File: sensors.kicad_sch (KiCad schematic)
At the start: 68 parts, among them J1 1-4, J2 5-8, Q1 2N3906, U1 ADG707, U2 OPA2340, U3 OPA2340

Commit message: changes for layout
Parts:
- removed Q1: 2N3906, Package_TO_SOT_THT:TO-92_Inline, symbol Transistor_BJT:2N3906
- added Q1: MMBT3906, Package_TO_SOT_SMD:SOT-23, symbol Transistor_BJT:MMBT3906
- R1, R10, R11, R12, R13, R14, R15, R16, R2, R3, R4, R5, R6, R7, R8, R9: footprint (none) -> Resistor_SMD:R_0603_1608Metric_Pad0.98x0.95mm_HandSolder
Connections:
- net +3V3: now also Q1.2 (E)
- net SENSOR_READY: now also Q1.3 (C)
- net at R18.2, U1.28 (DA): now also U2.3 (+); no longer U2.5 (+)
- net at R25.2: now also Q1.1 (B)
- net at R17.2, U1.2 (DB): now also U2.5 (+); no longer U2.3 (+)
- new net: R20.1, U2.1, U2.2 (-)
- new net: R19.1, U2.6 (-), U2.7
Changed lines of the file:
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@@
     (pin "2")
   )
-  (symbol (lib_id "Amplifier_Operational:OPA2340") (at 157.48 115.57 0) (unit 2)
+  (symbol (lib_id "Amplifier_Operational:OPA2340") (at 157.48 115.57 0) (unit 1)
     (in_bom yes) (on_board yes)
     (property "Reference" "U2" (id 0) (at 158.75 109.22 0))
@@
       (effects (font (size 1.27 1.27)) (justify left))
     )
-    (property "Footprint" "" (id 2) (at 78.232 184.15 90)
+    (property "Footprint" "Resistor_SMD:R_0603_1608Metric_Pad0.98x0.95mm_HandSolder" (id 2) (at 78.232 184.15 90)
       (effects (font (size 1.27 1.27)) hide)
     )
@@
     (pin "1")
     (pin "2")
+  )
+  (symbol (lib_id "Transistor_BJT:MMBT3906") (at 237.49 125.73 0) (mirror x) (unit 1)
+    (in_bom yes) (on_board yes)
+    (property "Reference" "Q1" (id 0) (at 228.6 128.27 0)
+      (effects (font (size 1.27 1.27)) (justify left))
+    )
+    (property "Value" "MMBT3906" (id 1) (at 228.6 130.81 0)
+      (effects (font (size 1.27 1.27)) (justify left))
+    )
+    (property "Footprint" "Package_TO_SOT_SMD:SOT-23" (id 2) (at 242.57 123.825 0)
+      (effects (font (size 1.27 1.27) italic) (justify left) hide)
+    )
+    (property "Datasheet" "https://www.onsemi.com/pub/Collateral/2N3906-D.PDF" (id 3) (at 237.49 125.73 0)
+      (effects (font (size 1.27 1.27)) (justify left) hide)
+    )
+    (pin "1")
+    (pin "2")
+    (pin "3")
   )
   (symbol (lib_id "power:+3V3") (at 128.27 82.55 0) (unit 1)
@@
       (effects (font (size 1.27 1.27)) (justify left))
     )
-    (property "Footprint" "" (id 2) (at 78.232 21.59 90)
+    (property "Footprint" "Resistor_SMD:R_0603_1608Metric_Pad0.98x0.95mm_HandSolder" (id 2) (at 78.232 21.59 90)
       (effects (font (size 1.27 1.27)) hide)
     )
@@
     (pin "2")
   )
-  (symbol (lib_id "Transistor_BJT:2N3906") (at 237.49 125.73 0) (mirror x) (unit 1)
-    (in_bom yes) (on_board yes)
-    (property "Reference" "Q1" (id 0) (at 229.87 129.54 0)
-      (effects (font (size 1.27 1.27)) (justify left))
-    )
-    (property "Value" "2N3906" (id 1) (at 229.87 132.08 0)
-      (effects (font (size 1.27 1.27)) (justify left))
-    )
-    (property "Footprint" "Package_TO_SOT_THT:TO-92_Inline" (id 2) (at 242.57 123.825 0)
-      (effects (font (size 1.27 1.27) italic) (justify left) hide)
-    )
-    (property "Datasheet" "https://www.onsemi.com/pub/Collateral/2N3906-D.PDF" (id 3) (at 237.49 125.73 0)
-      (effects (font (size 1.27 1.27)) (justify left) hide)
-    )
-    (pin "1")
-    (pin "2")
-    (pin "3")
-  )
   (symbol (lib_id "Device:R") (at 80.01 86.36 0) (unit 1)
     (in_bom yes) (on_board yes) (fields_autoplaced)
@@
       (effects (font (size 1.27 1.27)) (justify left))
     )
-    (property "Footprint" "" (id 2) (at 78.232 86.36 90)
+    (property "Footprint" "Resistor_SMD:R_0603_1608Metric_Pad0.98x0.95mm_HandSolder" (id 2) (at 78.232 86.36 90)
       (effects (font (size 1.27 1.27)) hide)
     )
@@
       (effects (font (size 1.27 1.27)) (justify left))
     )
-    (property "Footprint" "" (id 2) (at 78.232 162.56 90)
+    (property "Footprint" "Resistor_SMD:R_0603_1608Metric_Pad0.98x0.95mm_HandSolder" (id 2) (at 78.232 162.56 90)
       (effects (font (size 1.27 1.27)) hide)
     )
@@
       (effects (font (size 1.27 1.27)) (justify left))
     )
-    (property "Footprint" "" (id 2) (at 78.232 43.18 90)
+    (property "Footprint" "Resistor_SMD:R_0603_1608Metric_Pad0.98x0.95mm_HandSolder" (id 2) (at 78.232 43.18 90)
       (effects (font (size 1.27 1.27)) hide)
     )
@@
     (pin "9")
   )
-  (symbol (lib_id "Amplifier_Operational:OPA2340") (at 157.48 97.79 0) (unit 1)
+  (symbol (lib_id "Amplifier_Operational:OPA2340") (at 157.48 97.79 0) (unit 2)
     (in_bom yes) (on_board yes)
     (property "Reference" "U2" (id 0) (at 158.75 88.9 0))
@@
       (effects (font (size 1.27 1.27)) (justify left))
     )
-    (property "Footprint" "" (id 2) (at 78.232 97.79 90)
+    (property "Footprint" "Resistor_SMD:R_0603_1608Metric_Pad0.98x0.95mm_HandSolder" (id 2) (at 78.232 97.79 90)
       (effects (font (size 1.27 1.27)) hide)
     )
@@
       (effects (font (size 1.27 1.27)) (justify left))
     )
-    (property "Footprint" "" (id 2) (at 78.232 151.13 90)
+    (property "Footprint" "Resistor_SMD:R_0603_1608Metric_Pad0.98x0.95mm_HandSolder" (id 2) (at 78.232 151.13 90)
       (effects (font (size 1.27 1.27)) hide)
     )
@@
       (effects (font (size 1.27 1.27)) (justify left))
     )
-    (property "Footprint" "" (id 2) (at 78.232 33.02 90)
+    (property "Footprint" "Resistor_SMD:R_0603_1608Metric_Pad0.98x0.95mm_HandSolder" (id 2) (at 78.232 33.02 90)
       (effects (font (size 1.27 1.27)) hide)
     )
@@
       (effects (font (size 1.27 1.27)) (justify left))
     )
-    (property "Footprint" "" (id 2) (at 78.232 64.77 90)
+    (property "Footprint" "Resistor_SMD:R_0603_1608Metric_Pad0.98x0.95mm_HandSolder" (id 2) (at 78.232 64.77 90)
       (effects (font (size 1.27 1.27)) hide)
     )
@@
       (effects (font (size 1.27 1.27)) (justify left))
     )
-    (property "Footprint" "" (id 2) (at 78.232 76.2 90)
+    (property "Footprint" "Resistor_SMD:R_0603_1608Metric_Pad0.98x0.95mm_HandSolder" (id 2) (at 78.232 76.2 90)
       (effects (font (size 1.27 1.27)) hide)
     )
@@
       (effects (font (size 1.27 1.27)) (justify left))
     )
-    (property "Footprint" "" (id 2) (at 78.232 107.95 90)
+    (property "Footprint" "Resistor_SMD:R_0603_1608Metric_Pad0.98x0.95mm_HandSolder" (id 2) (at 78.232 107.95 90)
       (effects (font (size 1.27 1.27)) hide)
     )
@@
       (effects (font (size 1.27 1.27)) (justify left))
     )
-    (property "Footprint" "" (id 2) (at 78.232 54.61 90)
+    (property "Footprint" "Resistor_SMD:R_0603_1608Metric_Pad0.98x0.95mm_HandSolder" (id 2) (at 78.232 54.61 90)
       (effects (font (size 1.27 1.27)) hide)
     )
@@
       (effects (font (size 1.27 1.27)) (justify left))
     )
-    (property "Footprint" "" (id 2) (at 78.232 129.54 90)
+    (property "Footprint" "Resistor_SMD:R_0603_1608Metric_Pad0.98x0.95mm_HandSolder" (id 2) (at 78.232 129.54 90)
       (effects (font (size 1.27 1.27)) hide)
     )
@@
       (effects (font (size 1.27 1.27)) (justify left))
     )
-    (property "Footprint" "" (id 2) (at 78.232 172.72 90)
+    (property "Footprint" "Resistor_SMD:R_0603_1608Metric_Pad0.98x0.95mm_HandSolder" (id 2) (at 78.232 172.72 90)
       (effects (font (size 1.27 1.27)) hide)
     )
@@
       (effects (font (size 1.27 1.27)) (justify left))
     )
-    (property "Footprint" "" (id 2) (at 78.232 119.38 90)
+    (property "Footprint" "Resistor_SMD:R_0603_1608Metric_Pad0.98x0.95mm_HandSolder" (id 2) (at 78.232 119.38 90)
       (effects (font (size 1.27 1.27)) hide)
     )
@@
       (effects (font (size 1.27 1.27)) (justify left))
     )
-    (property "Footprint" "" (id 2) (at 78.232 140.97 90)
-      (effects (font (size 1.27 1.27)) hide)
-    )
+    (property "Footprint" "Resistor_SMD:R_0603_1608Metric_Pad0.98x0.95mm_HandSolder" (id 2) (at 78.232 140.97 90)
+      (effects (font (size 1.27 1.27)) hide)
+    )

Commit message: added some part numbers
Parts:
- U2, U3: Digikey (none) -> 296-26253-1-ND
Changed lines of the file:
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@@
+      (effects (font (size 1.27 1.27)) hide)
+    )
+    (property "Digikey" "296-26253-1-ND" (id 4) (at 157.48 97.79 0)
       (effects (font (size 1.27 1.27)) hide)
     )
@@
       (effects (font (size 1.27 1.27)) hide)
     )
+    (property "Digikey" "296-26253-1-ND" (id 4) (at 191.77 105.41 0)
+      (effects (font (size 1.27 1.27)) hide)
+    )
     (pin "1")
     (pin "2")
@@
     )
     (property "Datasheet" "http://www.ti.com/lit/ds/symlink/opa4340.pdf" (id 3) (at 157.48 148.59 0)
+      (effects (font (size 1.27 1.27)) hide)
+    )
+    (property "Digikey" "296-26253-1-ND" (id 4) (at 157.48 97.79 0)
       (effects (font (size 1.27 1.27)) hide)
     )
@@
       (effects (font (size 1.27 1.27)) hide)
     )
+    (property "Digikey" "296-26253-1-ND" (id 4) (at 157.48 97.79 0)
+      (effects (font (size 1.27 1.27)) hide)
+    )
     (pin "1")
     (pin "2")
@@
       (effects (font (size 1.27 1.27)) hide)
     )
+    (property "Digikey" "296-26253-1-ND" (id 4) (at 191.77 105.41 0)
+      (effects (font (size 1.27 1.27)) hide)
+    )
     (pin "1")
     (pin "2")
@@
       (effects (font (size 1.27 1.27)) hide)
     )
+    (property "Digikey" "296-26253-1-ND" (id 4) (at 191.77 105.41 0)
+      (effects (font (size 1.27 1.27)) hide)
+    )

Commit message: add copyright notices
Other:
- note added: "Copyright (C) 2023"
- note added: "Jonathan Bagg"
- note added: "SOLAR CONTROLLER 2023 - LMT01 Multiplexer"
- note added: "See https://creativecommons.org/licenses/by-nc-sa/4.0/"
- note added: "v1"

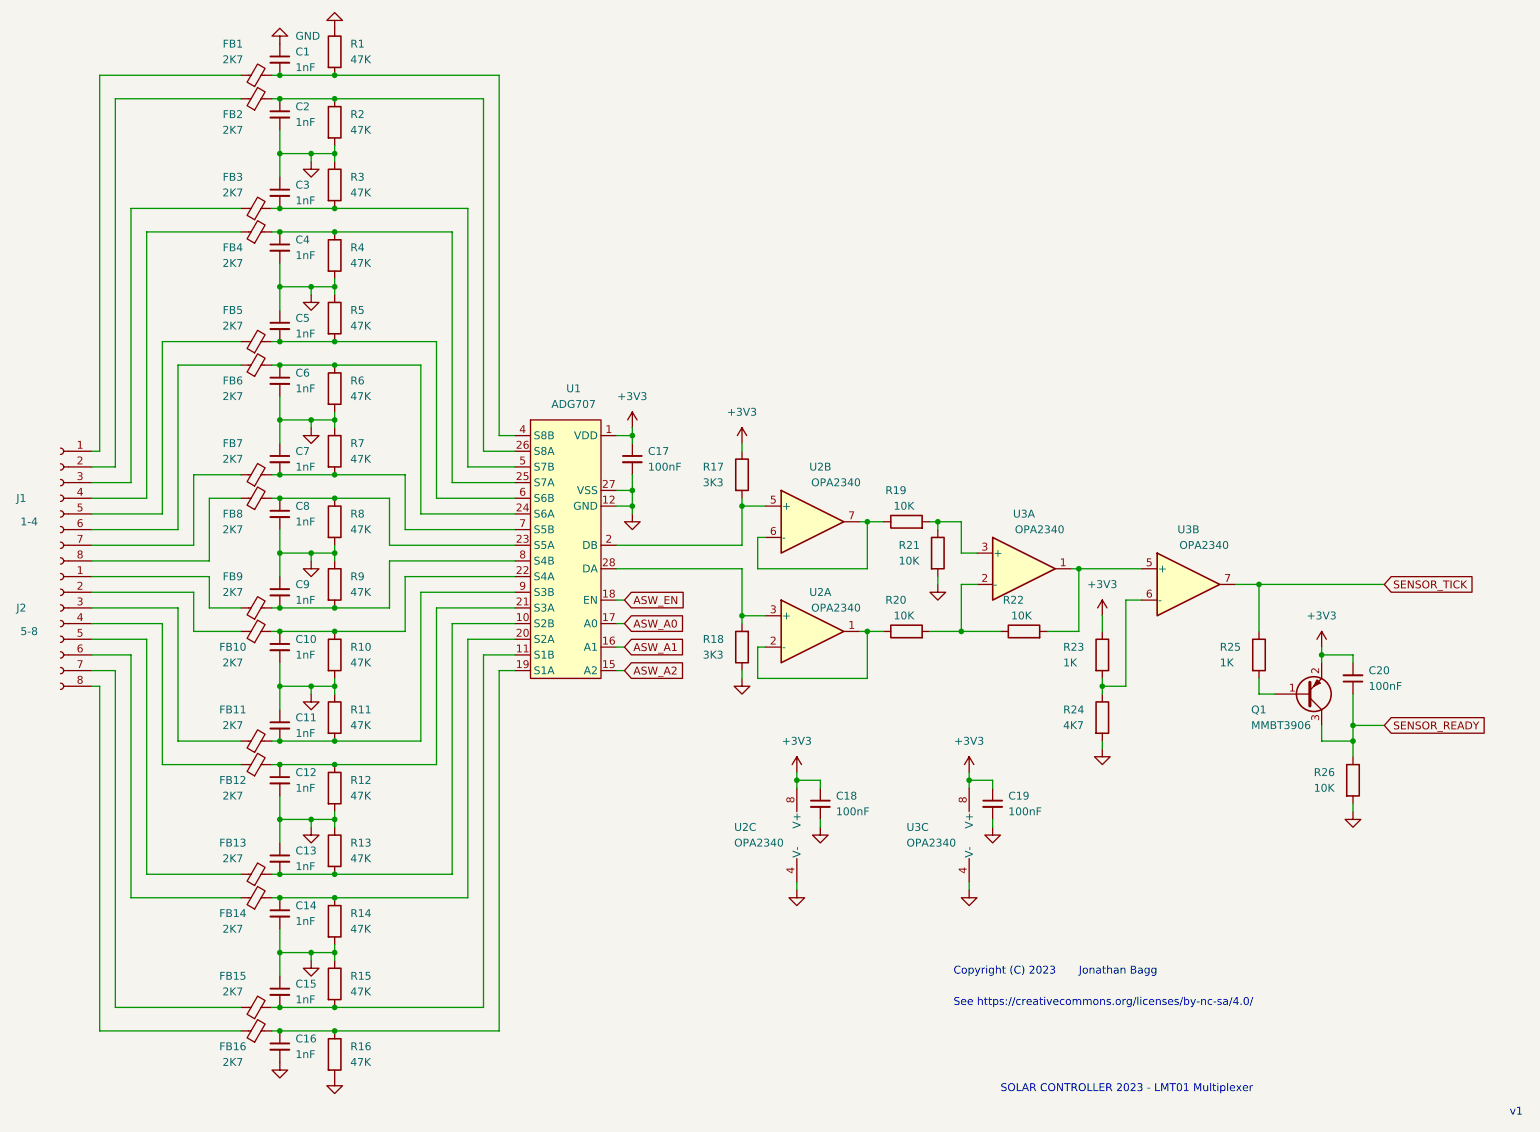
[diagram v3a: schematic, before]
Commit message: AC couple LMT01 signal conditioning and add gain
The difference circuit U3A was DC coupled and so could not
have gain.  Unit gain was only good for sensors up to 15m of
cat-5.
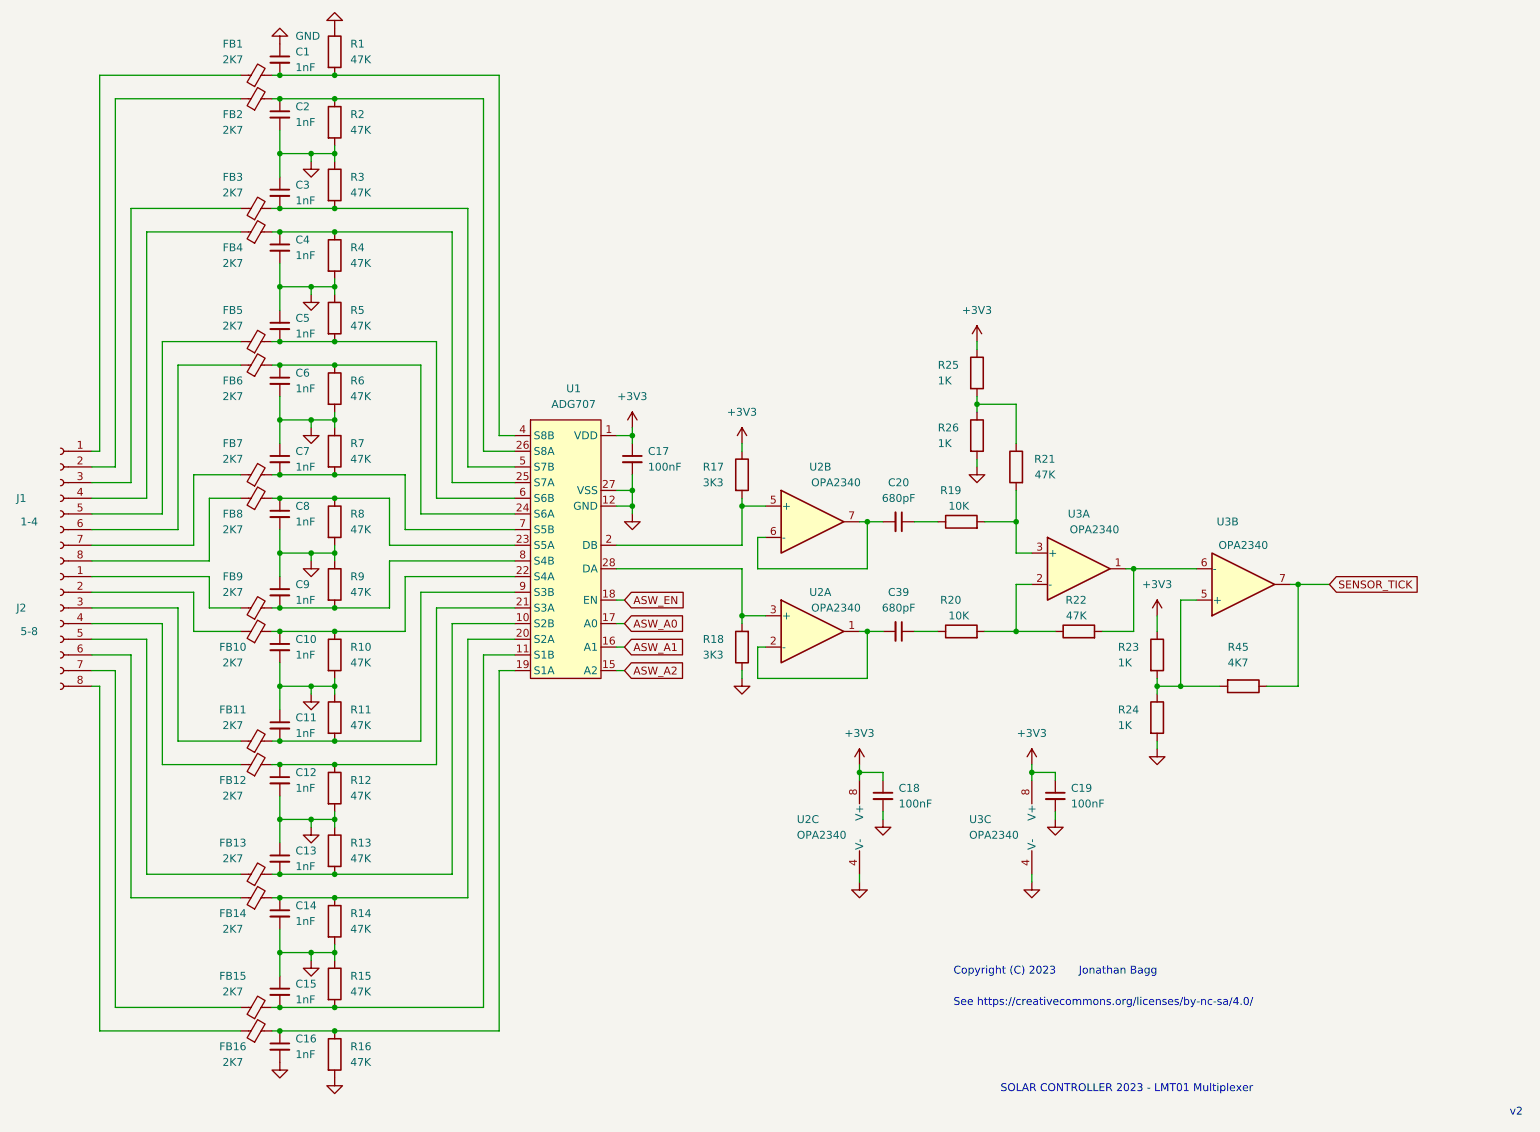
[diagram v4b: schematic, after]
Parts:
- removed Q1: MMBT3906, Package_TO_SOT_SMD:SOT-23, symbol Transistor_BJT:MMBT3906
- added C39: 680pF, Capacitor_SMD:C_0603_1608Metric_Pad1.08x0.95mm_HandSolder, symbol Device:C_Small
- added R45: 4K7, Resistor_SMD:R_0603_1608Metric_Pad0.98x0.95mm_HandSolder, symbol Device:R
- C20: value 100nF -> 680pF
- R21, R22: value 10K -> 47K
- R24: value 4K7 -> 1K
- R26: value 10K -> 1K
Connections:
- net +3V3: now also R25.1; no longer C20.2
- net GND: no longer R21.2
- net SENSOR_TICK: now also R45.1; no longer R25.1
- net at U2.1, U2.2 (-): now also C39.2; no longer R20.1
- net at R25.2: now also R21.1, R26.1
- net at U2.6 (-), U2.7: now also C20.2; no longer R19.1
- net at R19.2, U3.3 (+): now also R21.2; no longer R21.1
- net at R22.2, U3.1: now also U3.6 (-); no longer U3.5 (+)
- net at R23.2, R24.1: now also U3.5 (+), R45.2; no longer U3.6 (-)
- net SENSOR_READY: no longer names the net of C20.1
- net SENSOR_READY: now also R19.1; no longer R26.1
- new net: C39.1, R20.1
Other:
- note added: "v2"
- note removed: "v1"
- moved on the sheet: C18, C19, C20, R19, R20, R21, R22, R23, R24, R25, R26, U2C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
